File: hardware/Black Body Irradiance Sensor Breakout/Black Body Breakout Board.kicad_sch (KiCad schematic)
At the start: 6 parts, among them J2 Conn_01x05, U1 TSL25911FN

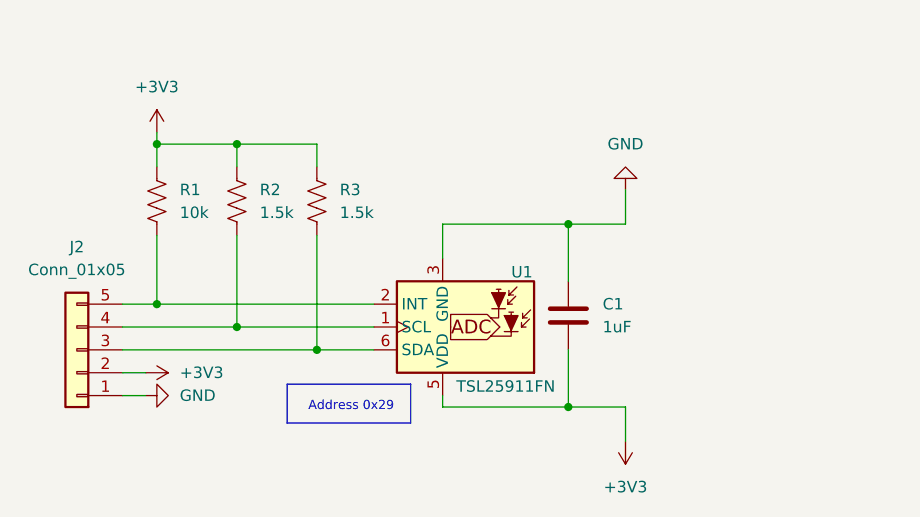
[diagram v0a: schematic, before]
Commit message: updated fuse silkscreen, added open circuit to TC
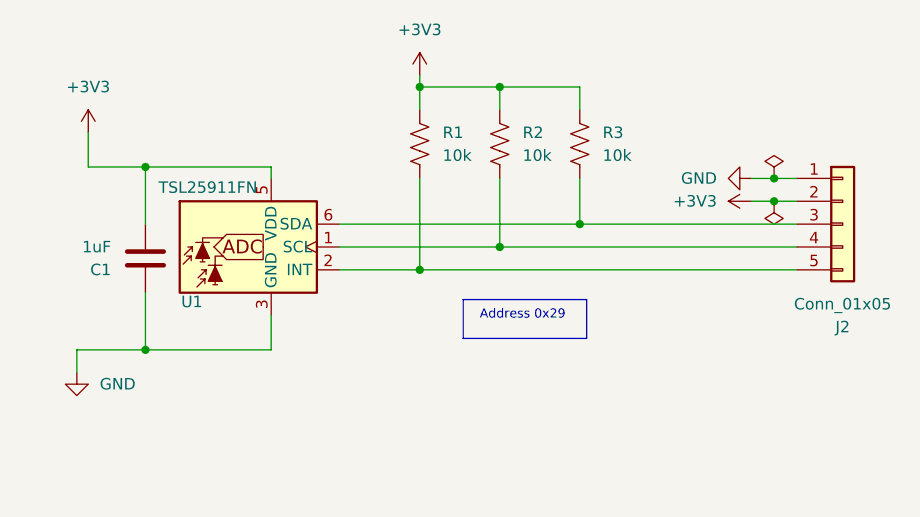
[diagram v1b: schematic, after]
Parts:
- R2, R3: value 1.5k -> 10k
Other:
- moved on the sheet: C1, J2, R1, R2, R3, U1

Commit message: updated cap
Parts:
- C1: footprint Capacitor_SMD:C_0805_2012Metric -> Capacitor_SMD:C_0201_0603Metric_Pad0.64x0.40mm_HandSolder
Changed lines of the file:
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@@
 			)
 		)
-		(property "Footprint" "Capacitor_SMD:C_0805_2012Metric"
+		(property "Footprint" "Capacitor_SMD:C_0201_0603Metric_Pad0.64x0.40mm_HandSolder"
 			(at 95.5548 74.93 0)
 			(effects

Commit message: updated resistors 0805 to 0603
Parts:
- C1: footprint Capacitor_SMD:C_0201_0603Metric_Pad0.64x0.40mm_HandSolder -> Capacitor_SMD:C_0603_1608Metric_Pad1.08x0.95mm_HandSolder
- R1, R2, R3: footprint Resistor_SMD:R_0805_2012Metric -> Resistor_SMD:R_0603_1608Metric_Pad0.98x0.95mm_HandSolder
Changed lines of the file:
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@@
 			)
 		)
-		(property "Footprint" "Resistor_SMD:R_0805_2012Metric"
+		(property "Footprint" "Resistor_SMD:R_0603_1608Metric_Pad0.98x0.95mm_HandSolder"
 			(at 145.796 66.294 90)
 			(effects
@@
 			)
 		)
-		(property "Footprint" "Resistor_SMD:R_0805_2012Metric"
+		(property "Footprint" "Resistor_SMD:R_0603_1608Metric_Pad0.98x0.95mm_HandSolder"
 			(at 136.906 66.294 90)
 			(effects
@@
 			)
 		)
-		(property "Footprint" "Resistor_SMD:R_0805_2012Metric"
+		(property "Footprint" "Resistor_SMD:R_0603_1608Metric_Pad0.98x0.95mm_HandSolder"
 			(at 128.016 66.294 90)
 			(effects
@@
 			)
 		)
-		(property "Footprint" "Capacitor_SMD:C_0201_0603Metric_Pad0.64x0.40mm_HandSolder"
+		(property "Footprint" "Capacitor_SMD:C_0603_1608Metric_Pad1.08x0.95mm_HandSolder"
 			(at 95.5548 74.93 0)
 			(effects
